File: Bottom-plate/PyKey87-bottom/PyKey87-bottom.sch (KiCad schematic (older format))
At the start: 8 parts

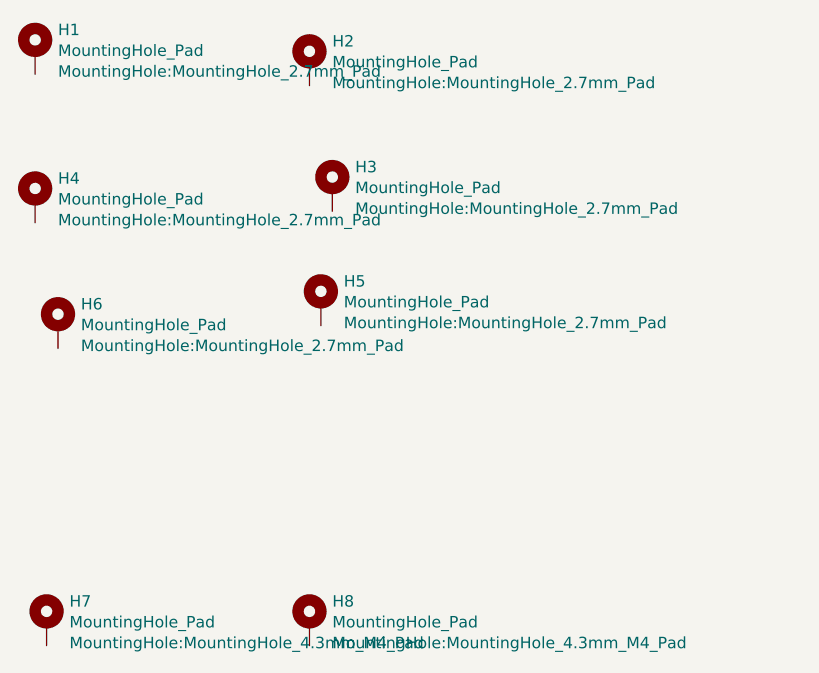
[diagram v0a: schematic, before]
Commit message: Add cutout for obscured switches
Also added extra holes for feet and additional standoff
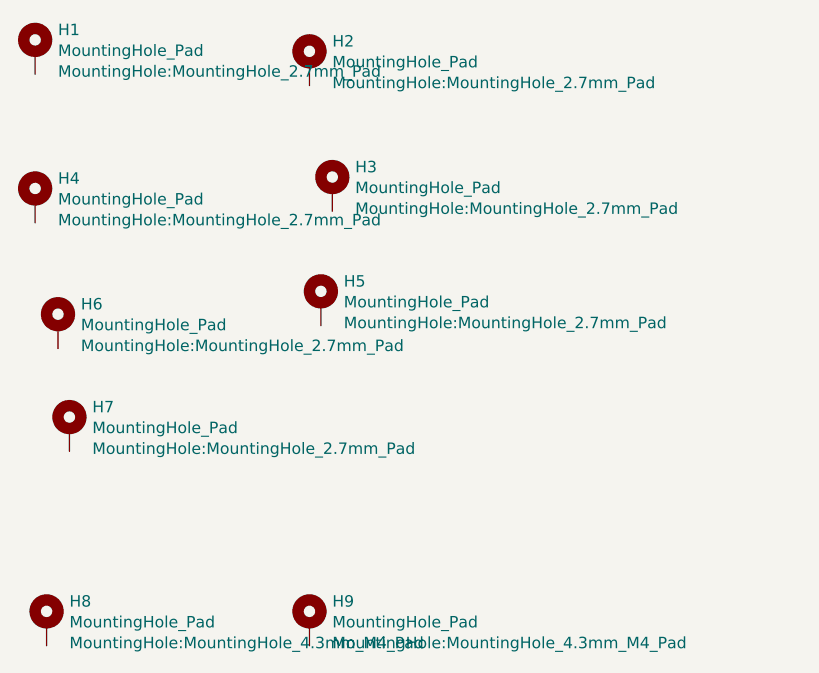
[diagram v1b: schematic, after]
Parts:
- added H7: MountingHole_Pad, MountingHole:MountingHole_2.7mm_Pad, symbol Mechanical:MountingHole_Pad
- renumbered H7 to H8, H8 to H9
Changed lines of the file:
@@
 EESchema Schematic File Version 4
+LIBS:PyKey87-bottom-cache
 EELAYER 29 0
 EELAYER END
@@
 $EndComp
 $Comp
-L Mechanical:MountingHole_Pad H7
+L Mechanical:MountingHole_Pad H8
 U 1 1 618E47BC
 P 2350 5000
-F 0 "H7" H 2450 5094 50  0000 L CNN
+F 0 "H8" H 2450 5094 50  0000 L CNN
 F 1 "MountingHole_Pad" H 2450 5003 50  0000 L CNN
 F 2 "MountingHole:MountingHole_4.3mm_M4_Pad" H 2450 4912 50  0000 L CNN
@@
 $EndComp
 $Comp
-L Mechanical:MountingHole_Pad H8
+L Mechanical:MountingHole_Pad H9
 U 1 1 618E4FDD
 P 3500 5000
-F 0 "H8" H 3600 5094 50  0000 L CNN
+F 0 "H9" H 3600 5094 50  0000 L CNN
 F 1 "MountingHole_Pad" H 3600 5003 50  0000 L CNN
 F 2 "MountingHole:MountingHole_4.3mm_M4_Pad" H 3600 4912 50  0000 L CNN
@@
 	1    0    0    -1
 $EndComp
+$Comp
+L Mechanical:MountingHole_Pad H7
+U 1 1 618ECBEC
+P 2450 4150
+F 0 "H7" H 2550 4244 50  0000 L CNN
+F 1 "MountingHole_Pad" H 2550 4153 50  0000 L CNN
+F 2 "MountingHole:MountingHole_2.7mm_Pad" H 2550 4062 50  0000 L CNN
+F 3 "~" H 2450 4150 50  0001 C CNN
+	1    2450 4150
+	1    0    0    -1
+$EndComp

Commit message: Shrink standoffs, enlarge cutout
added an additional standoff near G/H
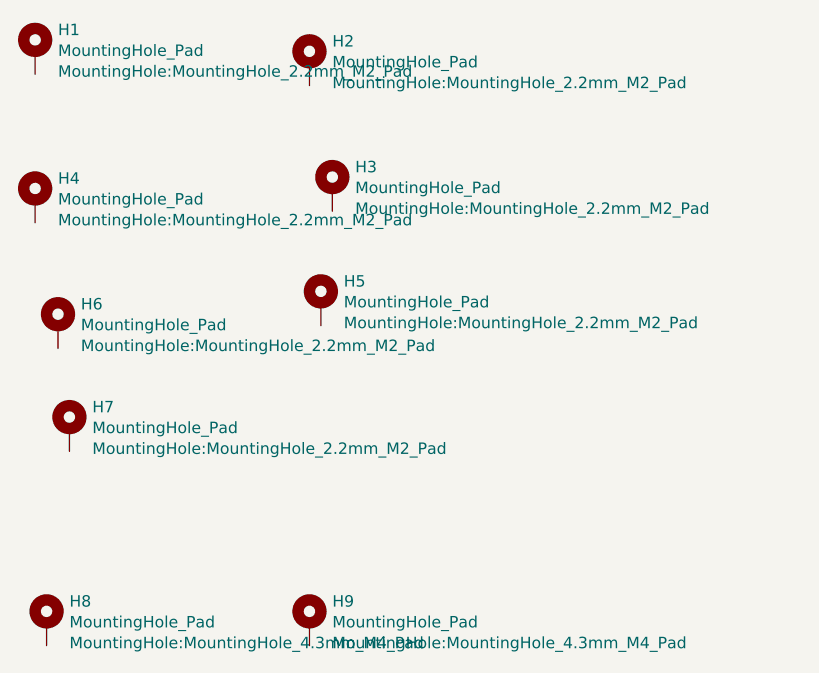
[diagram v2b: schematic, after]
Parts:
- H1, H2, H3, H4, H5, H6, H7: footprint MountingHole:MountingHole_2.7mm_Pad -> MountingHole:MountingHole_2.2mm_M2_Pad
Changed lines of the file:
@@
 F 0 "H2" H 3600 2644 50  0000 L CNN
 F 1 "MountingHole_Pad" H 3600 2553 50  0000 L CNN
-F 2 "MountingHole:MountingHole_2.7mm_Pad" H 3600 2462 50  0000 L CNN
+F 2 "MountingHole:MountingHole_2.2mm_M2_Pad" H 3600 2462 50  0000 L CNN
 F 3 "~" H 3500 2550 50  0001 C CNN
 	1    3500 2550
@@
 F 0 "H3" H 3700 3194 50  0000 L CNN
 F 1 "MountingHole_Pad" H 3700 3103 50  0000 L CNN
-F 2 "MountingHole:MountingHole_2.7mm_Pad" H 3700 3012 50  0000 L CNN
+F 2 "MountingHole:MountingHole_2.2mm_M2_Pad" H 3700 3012 50  0000 L CNN
 F 3 "~" H 3600 3100 50  0001 C CNN
 	1    3600 3100
@@
 F 0 "H5" H 3650 3694 50  0000 L CNN
 F 1 "MountingHole_Pad" H 3650 3603 50  0000 L CNN
-F 2 "MountingHole:MountingHole_2.7mm_Pad" H 3650 3512 50  0000 L CNN
+F 2 "MountingHole:MountingHole_2.2mm_M2_Pad" H 3650 3512 50  0000 L CNN
 F 3 "~" H 3550 3600 50  0001 C CNN
 	1    3550 3600
@@
 F 0 "H1" H 2400 2594 50  0000 L CNN
 F 1 "MountingHole_Pad" H 2400 2503 50  0000 L CNN
-F 2 "MountingHole:MountingHole_2.7mm_Pad" H 2400 2412 50  0000 L CNN
+F 2 "MountingHole:MountingHole_2.2mm_M2_Pad" H 2400 2412 50  0000 L CNN
 F 3 "~" H 2300 2500 50  0001 C CNN
 	1    2300 2500
@@
 F 0 "H4" H 2400 3244 50  0000 L CNN
 F 1 "MountingHole_Pad" H 2400 3153 50  0000 L CNN
-F 2 "MountingHole:MountingHole_2.7mm_Pad" H 2400 3062 50  0000 L CNN
+F 2 "MountingHole:MountingHole_2.2mm_M2_Pad" H 2400 3062 50  0000 L CNN
 F 3 "~" H 2300 3150 50  0001 C CNN
 	1    2300 3150
@@
 F 0 "H6" H 2500 3794 50  0000 L CNN
 F 1 "MountingHole_Pad" H 2500 3703 50  0000 L CNN
-F 2 "MountingHole:MountingHole_2.7mm_Pad" H 2500 3612 50  0000 L CNN
+F 2 "MountingHole:MountingHole_2.2mm_M2_Pad" H 2500 3612 50  0000 L CNN
 F 3 "~" H 2400 3700 50  0001 C CNN
 	1    2400 3700
@@
 F 0 "H7" H 2550 4244 50  0000 L CNN
 F 1 "MountingHole_Pad" H 2550 4153 50  0000 L CNN
-F 2 "MountingHole:MountingHole_2.7mm_Pad" H 2550 4062 50  0000 L CNN
+F 2 "MountingHole:MountingHole_2.2mm_M2_Pad" H 2550 4062 50  0000 L CNN
 F 3 "~" H 2450 4150 50  0001 C CNN
 	1    2450 4150
